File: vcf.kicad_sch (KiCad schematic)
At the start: 51 parts, among them J6 Conn_01x11_Pin, Q4 BC307, U19 Opamp_Dual, U24 LM13700, U25 LM13700

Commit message: Routing
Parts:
- R34, R35, R37, R44, R45, R51, R52, R53, R59: footprint Resistor_THT:R_Axial_DIN0207_L6.3mm_D2.5mm_P15.24mm_Horizontal -> Resistor_THT:R_Axial_DIN0309_L9.0mm_D3.2mm_P12.70mm_Horizontal
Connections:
- net +12V: now also RT18.3; no longer RT18.1
- net +15V: now also J6.10 (Pin_10); no longer J6.7 (Pin_7)
- net +5V: now also J6.11 (Pin_11)
- net -12V: now also RT18.1; no longer RT18.3
- net GND: now also RV15.1; no longer RV15.3
- net LFO_IN: now also RV15.3; no longer J6.8 (Pin_8), RV15.1
- net TRIGGER: now also J6.8 (Pin_8)
- net VCF_OUT: now also J6.7 (Pin_7), RT14.3; no longer J6.11 (Pin_11), RT14.1
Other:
- moved on the sheet: RV15
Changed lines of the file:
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@@
 	(wire
 		(pts
+			(xy 26.67 114.3) (xy 30.48 114.3)
+		)
+		(stroke
+			(width 0)
+			(type default)
+		)
+	)
+	(wire
+		(pts
 			(xy 208.28 53.34) (xy 219.71 53.34)
 		)
@@
 	(wire
 		(pts
+			(xy 41.91 22.86) (xy 48.26 22.86)
+		)
+		(stroke
+			(width 0)
+			(type default)
+		)
+	)
+	(wire
+		(pts
 			(xy 120.65 43.18) (xy 58.42 43.18)
 		)
@@
 	(wire
 		(pts
-			(xy 280.67 142.24) (xy 274.32 142.24)
+			(xy 57.15 22.86) (xy 59.69 22.86)
 		)
 		(stroke
@@
 	(wire
 		(pts
-			(xy 208.28 53.34) (xy 208.28 74.93)
+			(xy 280.67 142.24) (xy 274.32 142.24)
 		)
 		(stroke
@@
 	(wire
 		(pts
-			(xy 34.29 53.34) (xy 43.18 53.34)
+			(xy 208.28 53.34) (xy 208.28 74.93)
 		)
 		(stroke
@@
 	(wire
 		(pts
-			(xy 26.67 114.3) (xy 30.48 114.3)
+			(xy 34.29 53.34) (xy 43.18 53.34)
 		)
 		(stroke
@@
 		)
 	)
+	(label "GATE"
+		(at 26.67 104.14 180)
+		(effects
+			(font
+				(size 1.27 1.27)
+			)
+			(justify right bottom)
+		)
+	)
+	(label "TRIGGER"
+		(at 26.67 114.3 180)
+		(effects
+			(font
+				(size 1.27 1.27)
+			)
+			(justify right bottom)
+		)
+	)
 	(hierarchical_label "VCF_INPUT"
 		(shape input)
@@
 	(hierarchical_label "+5V"
 		(shape input)
-		(at 26.67 127 180)
+		(at 26.67 121.92 180)
 		(effects
 			(font
@@
 		)
 	)
-	(hierarchical_label "TRIGGER"
+	(hierarchical_label "+15V"
 		(shape input)
-		(at 26.67 124.46 180)
+		(at 57.15 22.86 180)
 		(effects
 			(font
@@
 	(hierarchical_label "LFO_IN"
 		(shape input)
-		(at 26.67 114.3 180)
+		(at 46.99 124.46 180)
 		(effects
 			(font
@@
 	(hierarchical_label "+15V"
 		(shape input)
-		(at 26.67 111.76 180)
+		(at 26.67 119.38 180)
 		(effects
 			(font
@@
 		)
 	)
-	(hierarchical_label "GATE"
+	(hierarchical_label "+5V"
 		(shape input)
-		(at 26.67 104.14 180)
+		(at 41.91 22.86 180)
 		(effects
 			(font
@@
 	(hierarchical_label "VCF_OUT"
 		(shape output)
-		(at 26.67 121.92 180)
+		(at 26.67 111.76 180)
 		(effects
 			(font
@@
 			)
 		)
-		(property "Footprint" "Resistor_THT:R_Axial_DIN0207_L6.3mm_D2.5mm_P15.24mm_Horizontal"
+		(property "Footprint" "Resistor_THT:R_Axial_DIN0309_L9.0mm_D3.2mm_P12.70mm_Horizontal"
 			(at 144.018 127 90)
 			(effects
@@
 			)
 		)
-		(property "Footprint" "Resistor_THT:R_Axial_DIN0207_L6.3mm_D2.5mm_P15.24mm_Horizontal"
+		(property "Footprint" "Resistor_THT:R_Axial_DIN0309_L9.0mm_D3.2mm_P12.70mm_Horizontal"
 			(at 72.39 68.072 90)
 			(effects
@@
 		(lib_id "Device:R_Potentiometer_Trim")
 		(at 207.01 144.78 0)
+		(mirror x)
 		(unit 1)
 		(exclude_from_sim no)
@@
 		(on_board yes)
 		(dnp no)
-		(fields_autoplaced yes)
 		(property "Reference" "RT14"
-			(at 204.47 143.5099 0)
+			(at 204.47 146.0501 0)
 			(effects
 				(font
@@
 		)
 		(property "Value" "100k"
-			(at 204.47 146.0499 0)
+			(at 204.47 143.5101 0)
 			(effects
 				(font
@@
 			)
 		)
-		(property "Footprint" "Resistor_THT:R_Axial_DIN0207_L6.3mm_D2.5mm_P15.24mm_Horizontal"
+		(property "Footprint" "Resistor_THT:R_Axial_DIN0309_L9.0mm_D3.2mm_P12.70mm_Horizontal"
 			(at 191.262 116.84 90)
 			(effects
@@
 		(lib_id "Device:R_Potentiometer_Trim")
 		(at 104.14 168.91 0)
+		(mirror x)
 		(unit 1)
 		(exclude_from_sim no)
@@
 		(on_board yes)
 		(dnp no)
+		(fields_autoplaced yes)
 		(property "Reference" "RT18"
 			(at 101.6 167.6399 0)
@@
 			)
 		)
-		(property "Footprint" "Resistor_THT:R_Axial_DIN0207_L6.3mm_D2.5mm_P15.24mm_Horizontal"
+		(property "Footprint" "Resistor_THT:R_Axial_DIN0309_L9.0mm_D3.2mm_P12.70mm_Horizontal"
 			(at 160.02 104.648 90)
 			(effects
@@
 			)
 		)
-		(property "Footprint" "Resistor_THT:R_Axial_DIN0207_L6.3mm_D2.5mm_P15.24mm_Horizontal"
+		(property "Footprint" "Resistor_THT:R_Axial_DIN0309_L9.0mm_D3.2mm_P12.70mm_Horizontal"
 			(at 78.232 78.74 90)
 			(effects
@@
 	)
 	(symbol
+		(lib_id "power:+5V")
+		(at 48.26 22.86 0)
+		(unit 1)
+		(exclude_from_sim no)
+		(in_bom yes)
+		(on_board yes)
+		(dnp no)
+		(fields_autoplaced yes)
+		(property "Reference" "#PWR0169"
+			(at 48.26 26.67 0)
+			(effects
+				(font
+					(size 1.27 1.27)
+				)
+				(hide yes)
+			)
+		)
+		(property "Value" "+5V"
+			(at 48.26 17.78 0)
+			(effects
+				(font
+					(size 1.27 1.27)
+				)
+			)
+		)
+		(property "Footprint" ""
+			(at 48.26 22.86 0)
+			(effects
+				(font
+					(size 1.27 1.27)
+				)
+				(hide yes)
+			)
+		)
+		(property "Datasheet" ""
+			(at 48.26 22.86 0)
+			(effects
+				(font
+					(size 1.27 1.27)
+				)
+				(hide yes)
+			)
+		)
+		(property "Description" "Power symbol creates a global label with name \"+5V\""
+			(at 48.26 22.86 0)
+			(effects
+				(font
+					(size 1.27 1.27)
+				)
+				(hide yes)
+			)
+		)
+		(pin "1"
+		)
+		(instances
+			(project "jensx1000"
+				(path "/3c53febc-5769-4c45-8f8f-0aba2c04e944/d9898a3a-269c-4039-8ec7-38b9f7f4aab4"
+					(reference "#PWR0169")
+					(unit 1)
+				)
+			)
+		)
+	)
+	(symbol
 		(lib_id "Device:R")
 		(at 185.42 69.85 270)
@@
 			)
 		)
-		(property "Footprint" "Resistor_THT:R_Axial_DIN0207_L6.3mm_D2.5mm_P15.24mm_Horizontal"
+		(property "Footprint" "Resistor_THT:R_Axial_DIN0309_L9.0mm_D3.2mm_P12.70mm_Horizontal"
 			(at 128.27 69.342 90)
 			(effects
@@
 			)
 		)
-		(property "Footprint" "Resistor_THT:R_Axial_DIN0207_L6.3mm_D2.5mm_P15.24mm_Horizontal"
+		(property "Footprint" "Resistor_THT:R_Axial_DIN0309_L9.0mm_D3.2mm_P12.70mm_Horizontal"
 			(at 181.61 104.648 90)
 			(effects
@@
 	)
 	(symbol
+		(lib_id "power:+15V")
+		(at 59.69 22.86 0)
+		(unit 1)
+		(exclude_from_sim no)
+		(in_bom yes)
+		(on_board yes)
+		(dnp no)
+		(fields_autoplaced yes)
+		(property "Reference" "#PWR0170"
+			(at 59.69 26.67 0)
+			(effects
+				(font
+					(size 1.27 1.27)
+				)
+				(hide yes)
+			)
+		)
+		(property "Value" "+15V"
+			(at 59.69 17.78 0)
+			(effects
+				(font
+					(size 1.27 1.27)
+				)
+			)
+		)
+		(property "Footprint" ""
+			(at 59.69 22.86 0)
+			(effects
+				(font
+					(size 1.27 1.27)
+				)
+				(hide yes)
+			)
+		)
+		(property "Datasheet" ""
+			(at 59.69 22.86 0)
+			(effects
+				(font
+					(size 1.27 1.27)
+				)
+				(hide yes)
+			)
+		)
+		(property "Description" "Power symbol creates a global label with name \"+15V\""
+			(at 59.69 22.86 0)
+			(effects
+				(font
+					(size 1.27 1.27)
+				)
+				(hide yes)
+			)
+		)
+		(pin "1"
+		)
+		(instances
+			(project "jensx1000"
+				(path "/3c53febc-5769-4c45-8f8f-0aba2c04e944/d9898a3a-269c-4039-8ec7-38b9f7f4aab4"
+					(reference "#PWR0170")
+					(unit 1)
+				)
+			)
+		)
+	)
+	(symbol
 		(lib_id "Device:R")
 		(at 203.2 53.34 90)
@@
 			)
 		)
-		(property "Footprint" "Resistor_THT:R_Axial_DIN0207_L6.3mm_D2.5mm_P15.24mm_Horizontal"
+		(property "Footprint" "Resistor_THT:R_Axial_DIN0309_L9.0mm_D3.2mm_P12.70mm_Horizontal"
 			(at 134.112 78.74 90)
 			(effects
@@
 	(symbol
 		(lib_id "Device:R_Potentiometer")
-		(at 162.56 153.67 0)
-		(mirror y)
+		(at 162.56 153.67 180)
 		(unit 1)
 		(exclude_from_sim no)
@@
 		(dnp no)
 		(property "Reference" "RV15"
-			(at 165.1 152.3999 0)
+			(at 165.1 154.9401 0)
 			(effects
 				(font
@@
 		)
 		(property "Value" "100kA"
-			(at 165.1 154.9399 0)
+			(at 165.1 152.4001 0)
 			(effects
 				(font
@@
 			)
 		)
-		(property "Footprint" "Resistor_THT:R_Axial_DIN0207_L6.3mm_D2.5mm_P15.24mm_Horizontal"
+		(property "Footprint" "Resistor_THT:R_Axial_DIN0309_L9.0mm_D3.2mm_P12.70mm_Horizontal"
 			(at 88.9 55.118 90)
 			(effects

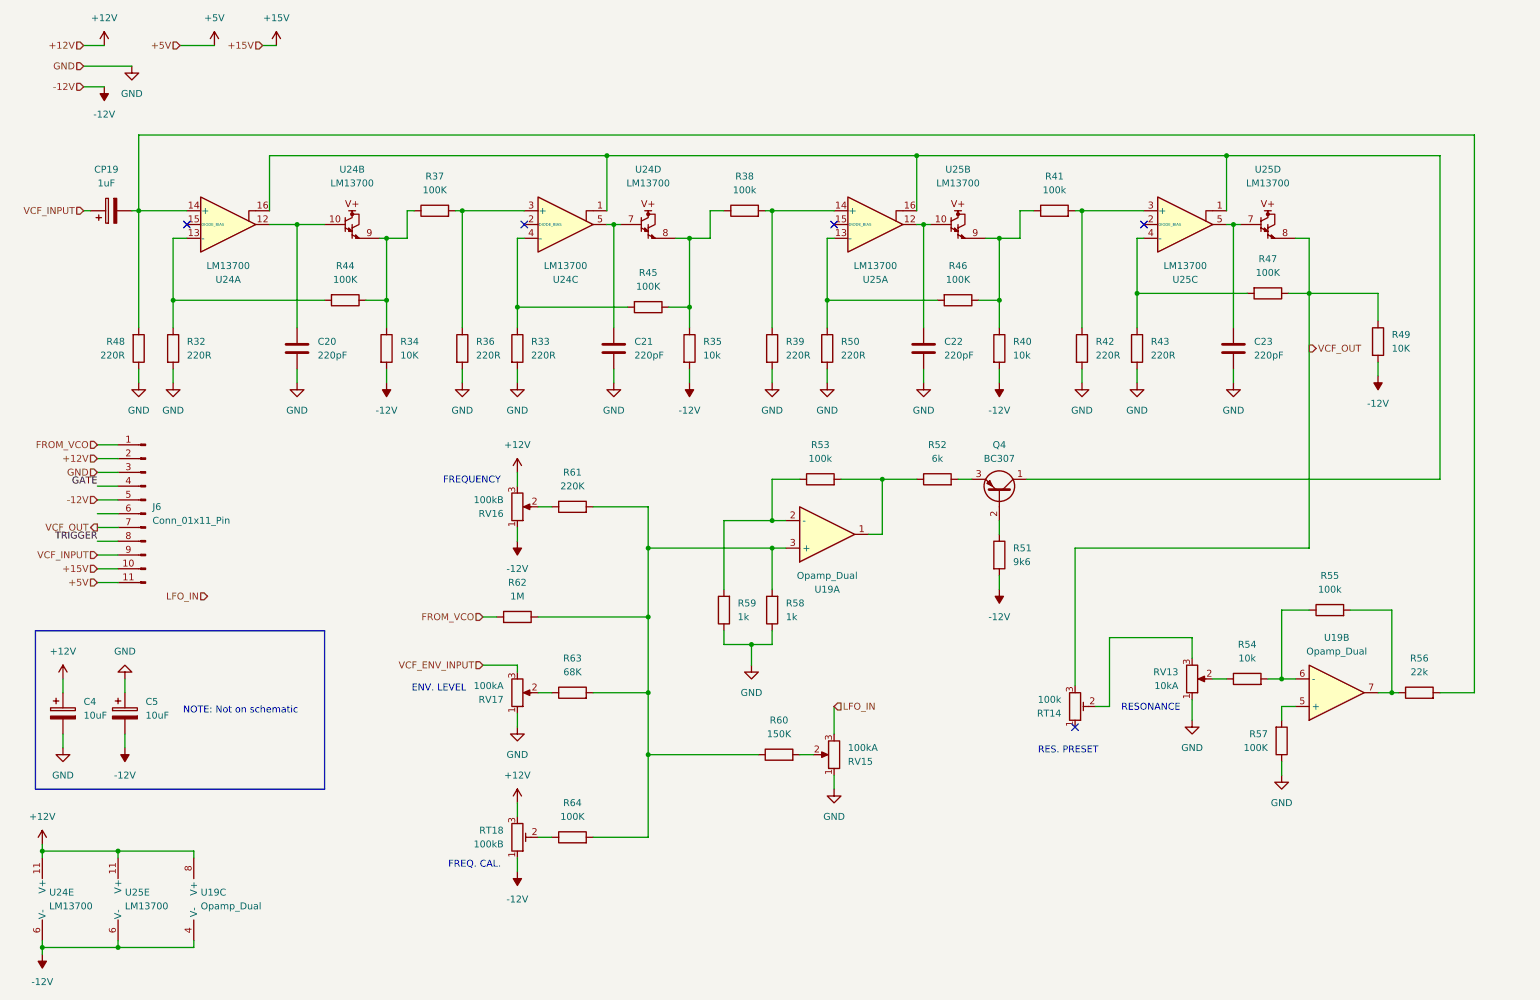
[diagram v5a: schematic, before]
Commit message: Fix VCF layout, routing, adding pads for switches
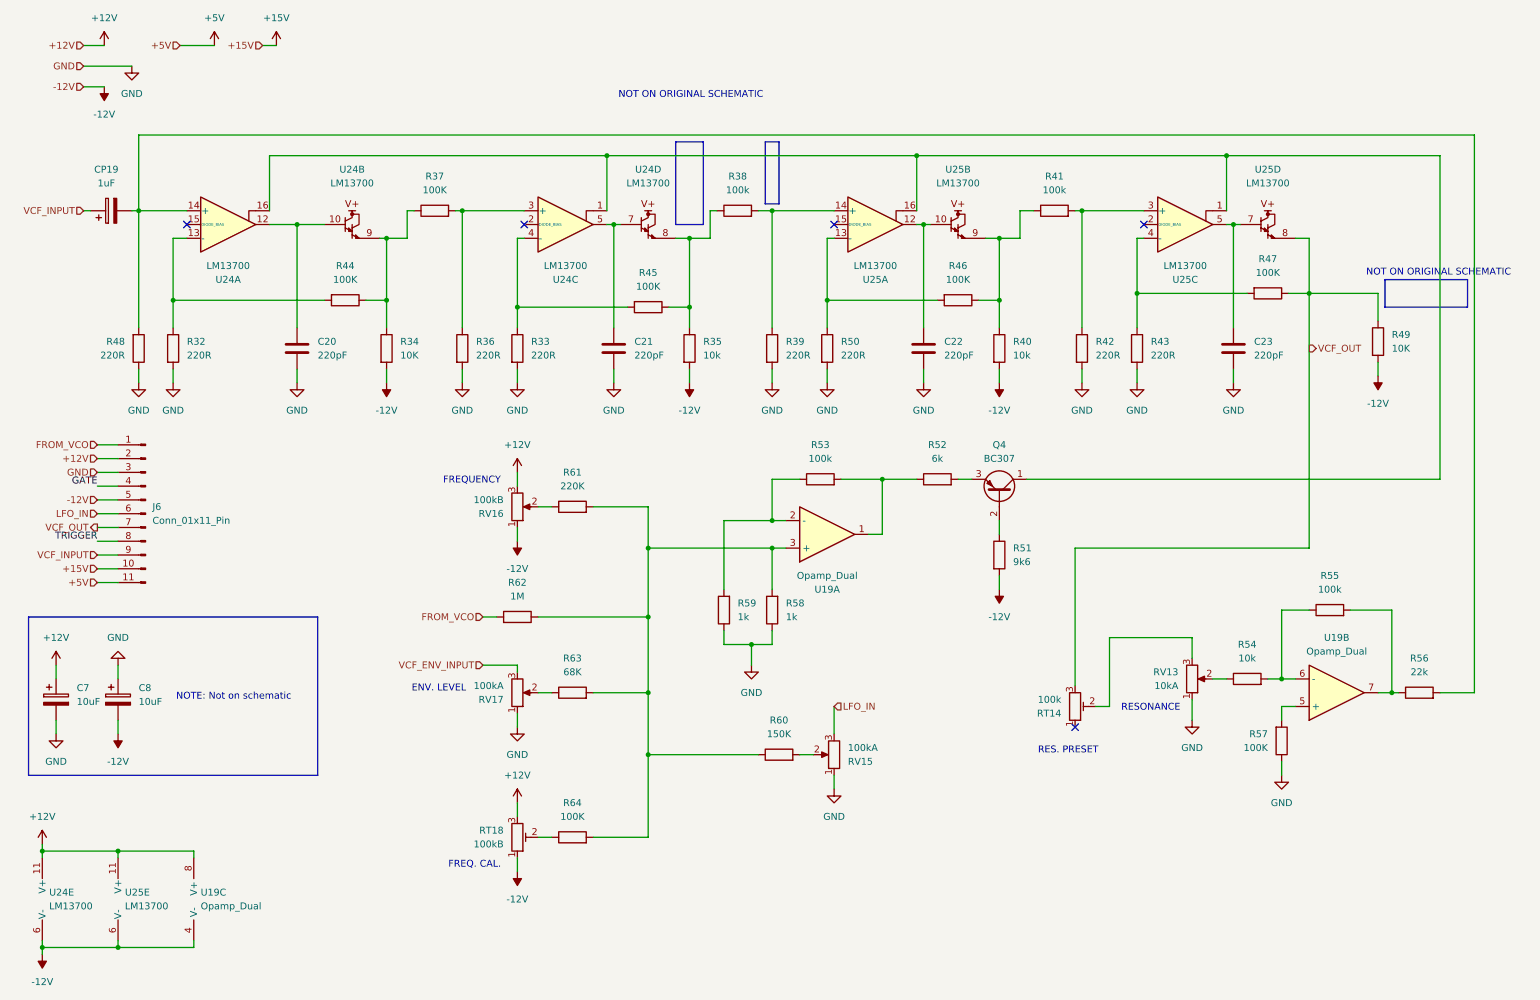
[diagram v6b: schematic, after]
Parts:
- removed C4, C5: 10uF, Capacitor_THT:CP_Radial_D8.0mm_P3.80mm, symbol Device:C_Polarized
- added C7, C8: 10uF, Capacitor_THT:CP_Radial_D8.0mm_P3.80mm, symbol Device:C_Polarized
- R39, R40, R41, R42, R43, R46, R47, R49, R50: footprint Resistor_THT:R_Axial_DIN0207_L6.3mm_D2.5mm_P15.24mm_Horizontal -> Resistor_THT:R_Axial_DIN0309_L9.0mm_D3.2mm_P12.70mm_Horizontal
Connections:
- net +12V: now also C7.1
- net -12V: now also C8.2
- net GND: now also C7.2, C8.1
- net LFO_IN: now also J6.6 (Pin_6)
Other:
- note added: "NOT ON ORIGINAL SCHEMATIC"
- moved on the sheet: R38

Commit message: Remove redundant notes
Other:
- note removed: "NOT ON ORIGINAL SCHEMATIC"
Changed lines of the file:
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@@
 	(paper "A4")
-	(rectangle
-		(start 133.35 40.64)
-		(end 138.43 55.88)
-		(stroke
-			(width 0)
-			(type default)
-		)
-		(fill
-			(type none)
-		)
-	)
-	(rectangle
-		(start 264.16 66.04)
-		(end 279.4 71.12)
-		(stroke
-			(width 0)
-			(type default)
-		)
-		(fill
-			(type none)
-		)
-	)
-	(rectangle
-		(start 149.86 40.64)
-		(end 152.4 52.07)
-		(stroke
-			(width 0)
-			(type default)
-		)
-		(fill
-			(type none)
-		)
-	)
 	(rectangle
 		(start 13.97 128.27)
@@
 		(exclude_from_sim no)
 		(at 89.662 141.478 0)
-		(effects
-			(font
-				(size 1.27 1.27)
-			)
-		)
-	)
-	(text "NOT ON ORIGINAL SCHEMATIC"
-		(exclude_from_sim no)
-		(at 274.066 64.77 0)
 		(effects
 			(font
@@
 		(effects
 			(font
-				(size 1.27 1.27)
-			)
-		)
-	)
-	(text "NOT ON ORIGINAL SCHEMATIC"
-		(exclude_from_sim no)
-		(at 136.144 32.004 0)
-		(effects
-			(font

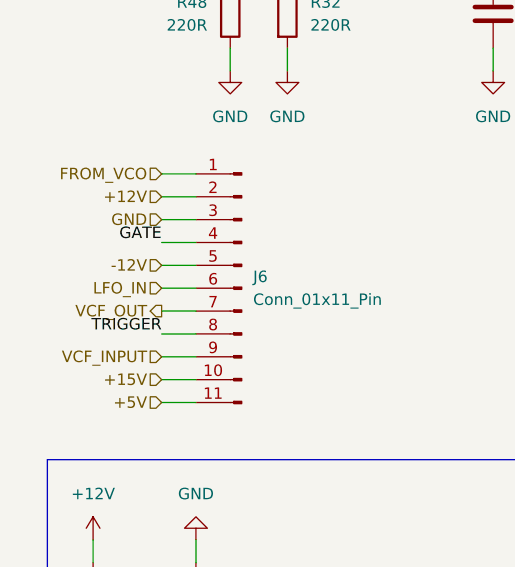
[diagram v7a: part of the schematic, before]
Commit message: Fixed VCF TRIG/GATE net, routed all except keyboard
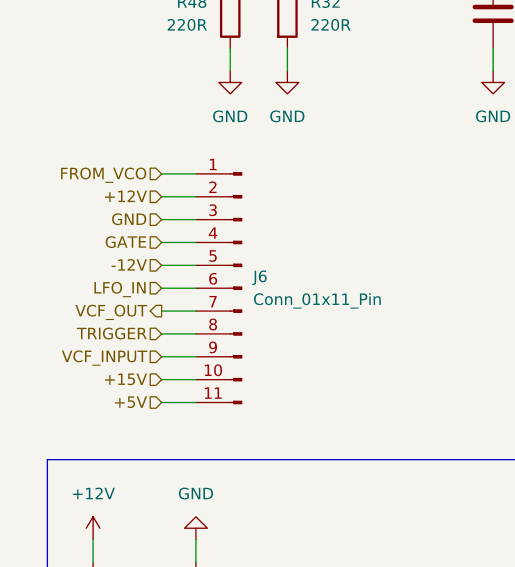
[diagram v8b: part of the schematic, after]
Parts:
- R32, R48: footprint Resistor_THT:R_Axial_DIN0207_L6.3mm_D2.5mm_P15.24mm_Horizontal -> Resistor_THT:R_Axial_DIN0207_L6.3mm_D2.5mm_P10.16mm_Horizontal
- R33, R36: footprint Resistor_THT:R_Axial_DIN0207_L6.3mm_D2.5mm_P15.24mm_Horizontal -> Resistor_THT:R_Axial_DIN0309_L9.0mm_D3.2mm_P12.70mm_Horizontal
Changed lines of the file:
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@@
-		)
-	)
-	(label "GATE"
-		(at 26.67 104.14 180)
-		(effects
-			(font
-				(size 1.27 1.27)
-			)
-			(justify right bottom)
-		)
-	)
-	(label "TRIGGER"
-		(at 26.67 114.3 180)
-		(effects
-			(font
-				(size 1.27 1.27)
-			)
-			(justify right bottom)
 		)
 	)
@@
 		)
 	)
+	(hierarchical_label "TRIGGER"
+		(shape input)
+		(at 26.67 114.3 180)
+		(effects
+			(font
+				(size 1.27 1.27)
+			)
+			(justify right)
+		)
+	)
 	(hierarchical_label "+15V"
 		(shape input)
@@
 		)
 	)
+	(hierarchical_label "GATE"
+		(shape input)
+		(at 26.67 104.14 180)
+		(effects
+			(font
+				(size 1.27 1.27)
+			)
+			(justify right)
+		)
+	)
 	(hierarchical_label "+15V"
 		(shape input)
@@
 			)
 		)
-		(property "Footprint" "Resistor_THT:R_Axial_DIN0207_L6.3mm_D2.5mm_P15.24mm_Horizontal"
+		(property "Footprint" "Resistor_THT:R_Axial_DIN0309_L9.0mm_D3.2mm_P12.70mm_Horizontal"
 			(at 102.362 78.74 90)
 			(effects
@@
 			)
 		)
-		(property "Footprint" "Resistor_THT:R_Axial_DIN0207_L6.3mm_D2.5mm_P15.24mm_Horizontal"
+		(property "Footprint" "Resistor_THT:R_Axial_DIN0207_L6.3mm_D2.5mm_P10.16mm_Horizontal"
 			(at 32.512 78.74 90)
 			(effects
@@
 			)
 		)
-		(property "Footprint" "Resistor_THT:R_Axial_DIN0207_L6.3mm_D2.5mm_P15.24mm_Horizontal"
+		(property "Footprint" "Resistor_THT:R_Axial_DIN0309_L9.0mm_D3.2mm_P12.70mm_Horizontal"
 			(at 92.202 78.74 90)
 			(effects
@@
 			)
 		)
-		(property "Footprint" "Resistor_THT:R_Axial_DIN0207_L6.3mm_D2.5mm_P15.24mm_Horizontal"
+		(property "Footprint" "Resistor_THT:R_Axial_DIN0207_L6.3mm_D2.5mm_P10.16mm_Horizontal"
 			(at 38.862 78.74 90)
 			(effects
